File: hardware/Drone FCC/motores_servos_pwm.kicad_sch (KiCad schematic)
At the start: 13 parts, among them J10 Conn_01x03, J11 Conn_01x03, J12 Conn_01x03, J13 Conn_01x03, J14 Conn_01x03, J16 Conn_01x02, J3 Conn_01x03, J4 Conn_01x03, J5 Conn_01x03, J6 Conn_01x03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

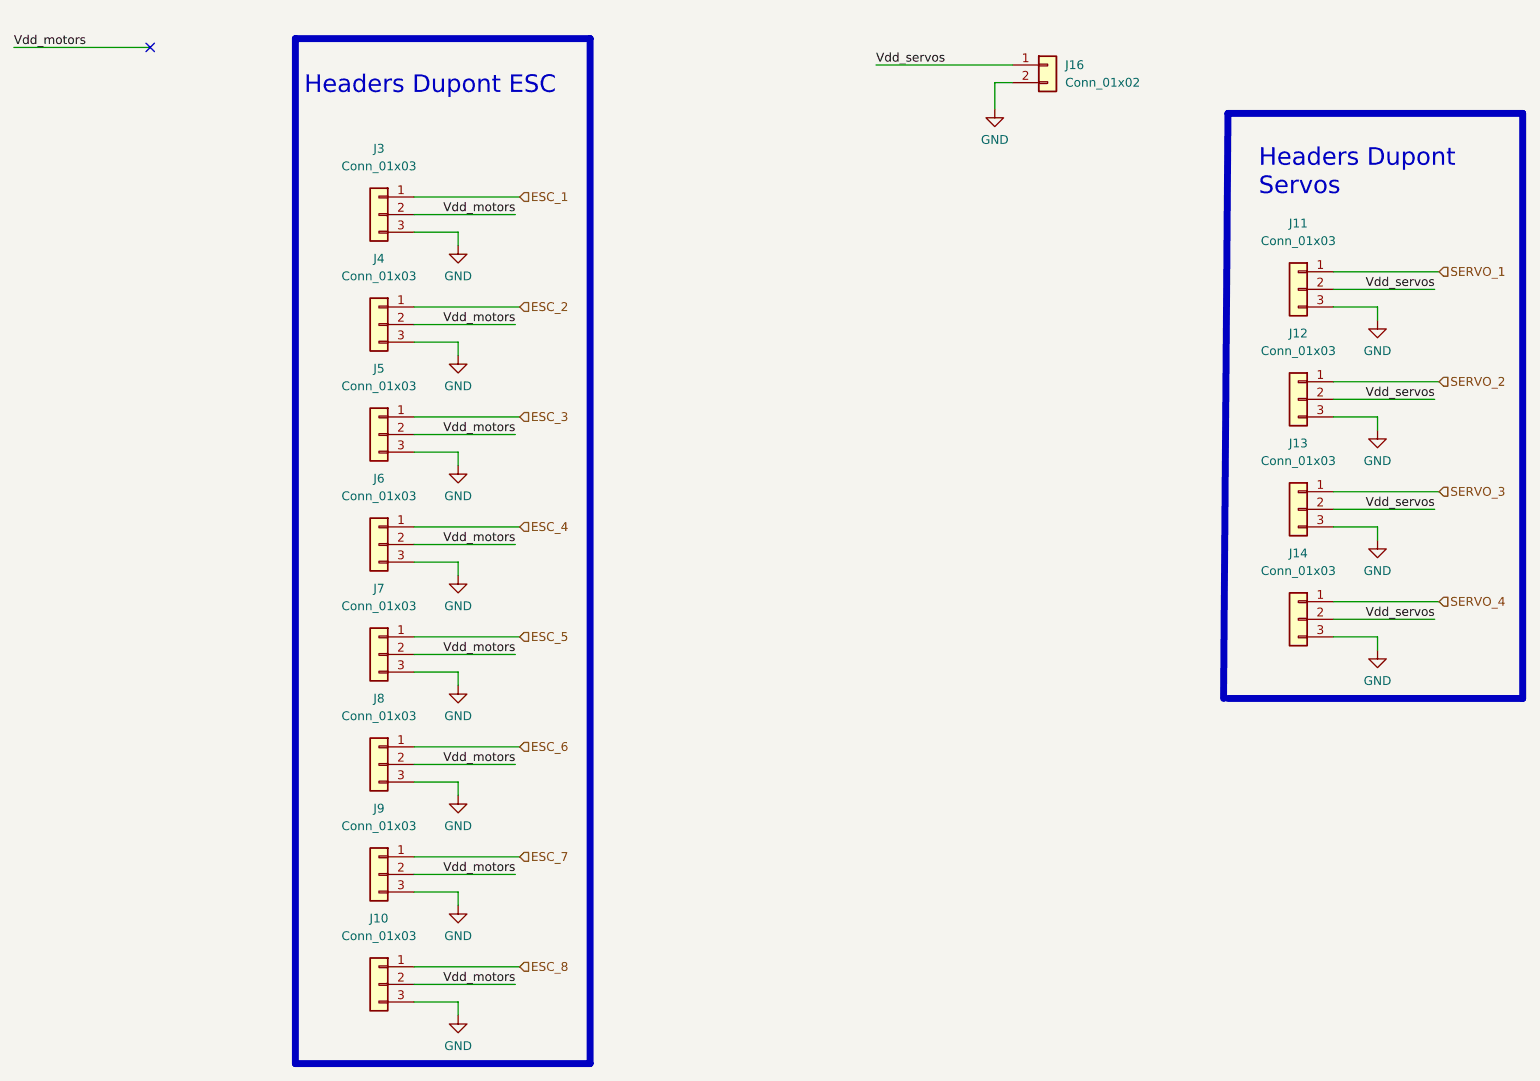
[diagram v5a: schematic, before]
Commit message: re enumeration of components
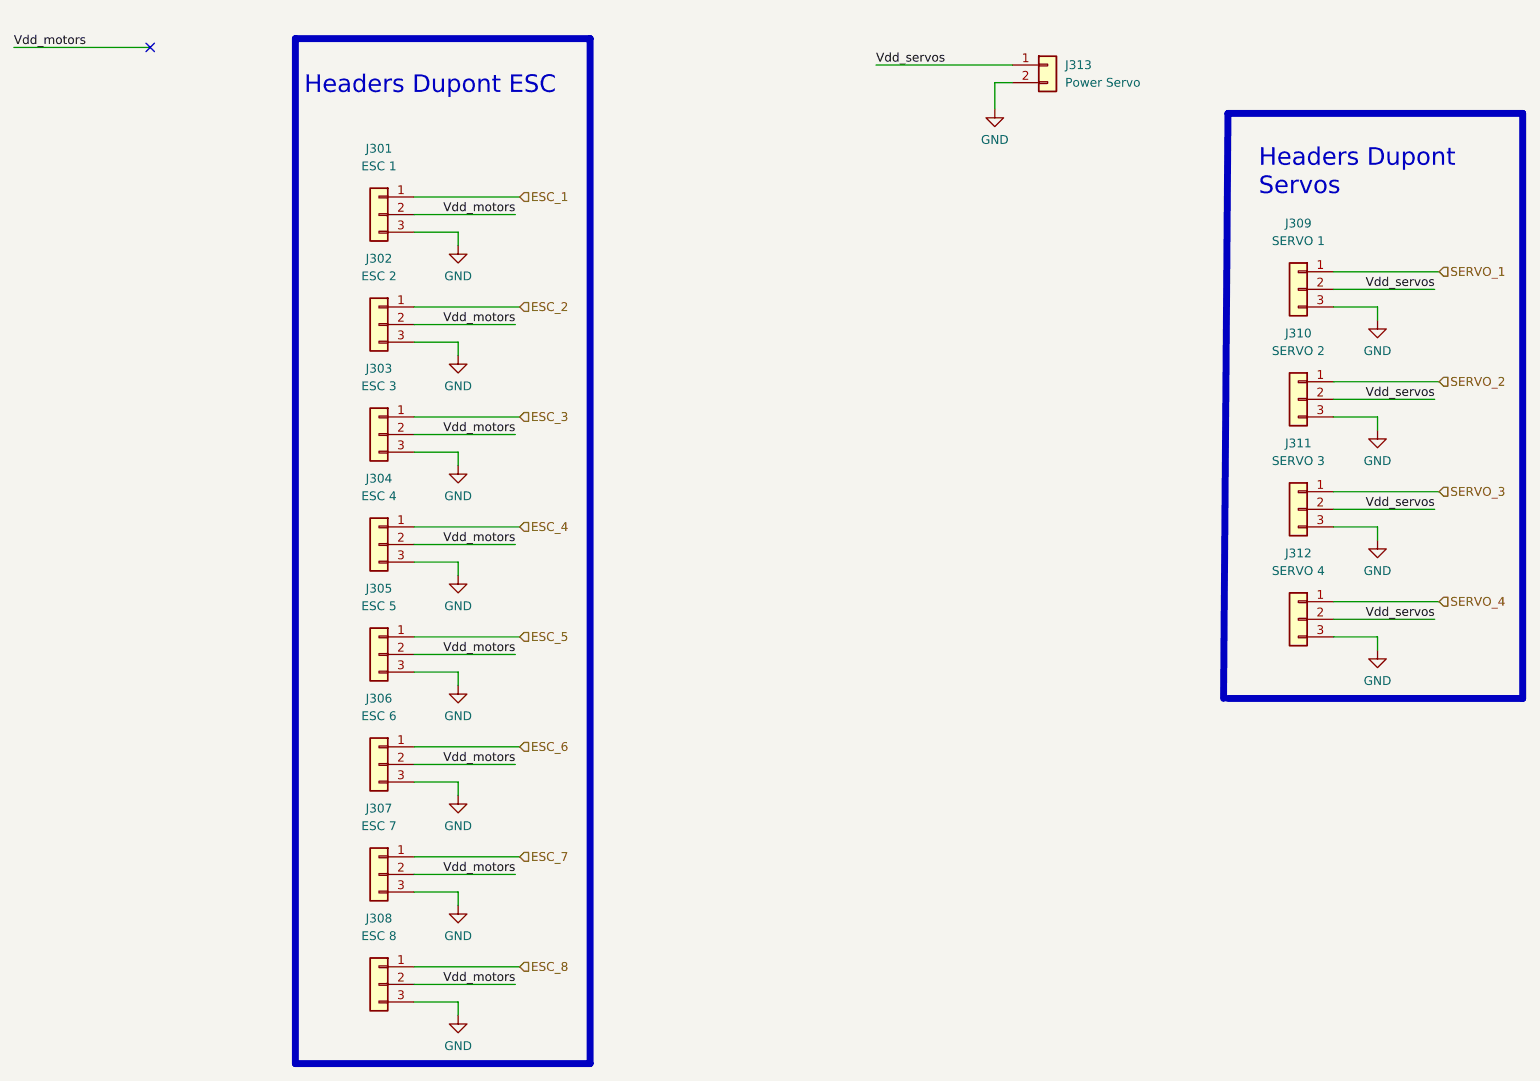
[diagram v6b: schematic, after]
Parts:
- J301: renamed from J3; value Conn_01x03 -> ESC 1
- J302: renamed from J4; value Conn_01x03 -> ESC 2
- J303: renamed from J5; value Conn_01x03 -> ESC 3
- J304: renamed from J6; value Conn_01x03 -> ESC 4
- J305: renamed from J7; value Conn_01x03 -> ESC 5
- J306: renamed from J8; value Conn_01x03 -> ESC 6
- J307: renamed from J9; value Conn_01x03 -> ESC 7
- J308: renamed from J10; value Conn_01x03 -> ESC 8
- J309: renamed from J11; value Conn_01x03 -> SERVO 1
- J310: renamed from J12; value Conn_01x03 -> SERVO 2
- J311: renamed from J13; value Conn_01x03 -> SERVO 3
- J312: renamed from J14; value Conn_01x03 -> SERVO 4
- J313: renamed from J16; value Conn_01x02 -> Power Servo
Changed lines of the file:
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@@
   (symbol (lib_id "Connector_Generic:Conn_01x03") (at 201.295 89.535 0) (mirror y) (unit 1)
     (in_bom yes) (on_board yes) (fields_autoplaced)
-    (property "Reference" "J13" (id 0) (at 201.295 80.01 0))
-    (property "Value" "Conn_01x03" (id 1) (at 201.295 82.55 0))
+    (property "Reference" "J311" (id 0) (at 201.295 80.01 0))
+    (property "Value" "SERVO 3" (id 1) (at 201.295 82.55 0))
     (property "Footprint" "TSW-101-08-G-T-RA:SAMTEC_TSW-101-08-G-T-RA" (id 2) (at 201.295 89.535 0)
       (effects (font (size 1.27 1.27)) hide)
@@
   (symbol (lib_id "Connector_Generic:Conn_01x03") (at 68.58 110.49 0) (mirror y) (unit 1)
     (in_bom yes) (on_board yes) (fields_autoplaced)
-    (property "Reference" "J7" (id 0) (at 68.58 100.965 0))
-    (property "Value" "Conn_01x03" (id 1) (at 68.58 103.505 0))
+    (property "Reference" "J305" (id 0) (at 68.58 100.965 0))
+    (property "Value" "ESC 5" (id 1) (at 68.58 103.505 0))
     (property "Footprint" "TSW-101-08-G-T-RA:SAMTEC_TSW-101-08-G-T-RA" (id 2) (at 68.58 110.49 0)
       (effects (font (size 1.27 1.27)) hide)
@@
   (symbol (lib_id "Connector_Generic:Conn_01x03") (at 68.58 46.99 0) (mirror y) (unit 1)
     (in_bom yes) (on_board yes) (fields_autoplaced)
-    (property "Reference" "J3" (id 0) (at 68.58 37.465 0))
-    (property "Value" "Conn_01x03" (id 1) (at 68.58 40.005 0))
+    (property "Reference" "J301" (id 0) (at 68.58 37.465 0))
+    (property "Value" "ESC 1" (id 1) (at 68.58 40.005 0))
     (property "Footprint" "TSW-101-08-G-T-RA:SAMTEC_TSW-101-08-G-T-RA" (id 2) (at 68.58 46.99 0)
       (effects (font (size 1.27 1.27)) hide)
@@
   (symbol (lib_id "Connector_Generic:Conn_01x03") (at 68.58 62.865 0) (mirror y) (unit 1)
     (in_bom yes) (on_board yes) (fields_autoplaced)
-    (property "Reference" "J4" (id 0) (at 68.58 53.34 0))
-    (property "Value" "Conn_01x03" (id 1) (at 68.58 55.88 0))
+    (property "Reference" "J302" (id 0) (at 68.58 53.34 0))
+    (property "Value" "ESC 2" (id 1) (at 68.58 55.88 0))
     (property "Footprint" "TSW-101-08-G-T-RA:SAMTEC_TSW-101-08-G-T-RA" (id 2) (at 68.58 62.865 0)
       (effects (font (size 1.27 1.27)) hide)
@@
   (symbol (lib_id "Connector_Generic:Conn_01x03") (at 201.295 105.41 0) (mirror y) (unit 1)
     (in_bom yes) (on_board yes) (fields_autoplaced)
-    (property "Reference" "J14" (id 0) (at 201.295 95.885 0))
-    (property "Value" "Conn_01x03" (id 1) (at 201.295 98.425 0))
+    (property "Reference" "J312" (id 0) (at 201.295 95.885 0))
+    (property "Value" "SERVO 4" (id 1) (at 201.295 98.425 0))
     (property "Footprint" "TSW-101-08-G-T-RA:SAMTEC_TSW-101-08-G-T-RA" (id 2) (at 201.295 105.41 0)
       (effects (font (size 1.27 1.27)) hide)
@@
   (symbol (lib_id "Connector_Generic:Conn_01x03") (at 68.58 78.74 0) (mirror y) (unit 1)
     (in_bom yes) (on_board yes) (fields_autoplaced)
-    (property "Reference" "J5" (id 0) (at 68.58 69.215 0))
-    (property "Value" "Conn_01x03" (id 1) (at 68.58 71.755 0))
+    (property "Reference" "J303" (id 0) (at 68.58 69.215 0))
+    (property "Value" "ESC 3" (id 1) (at 68.58 71.755 0))
     (property "Footprint" "TSW-101-08-G-T-RA:SAMTEC_TSW-101-08-G-T-RA" (id 2) (at 68.58 78.74 0)
       (effects (font (size 1.27 1.27)) hide)
@@
   (symbol (lib_id "Connector_Generic:Conn_01x03") (at 201.295 57.785 0) (mirror y) (unit 1)
     (in_bom yes) (on_board yes)
-    (property "Reference" "J11" (id 0) (at 201.295 48.26 0))
-    (property "Value" "Conn_01x03" (id 1) (at 201.295 50.8 0))
+    (property "Reference" "J309" (id 0) (at 201.295 48.26 0))
+    (property "Value" "SERVO 1" (id 1) (at 201.295 50.8 0))
     (property "Footprint" "TSW-101-08-G-T-RA:SAMTEC_TSW-101-08-G-T-RA" (id 2) (at 201.295 57.785 0)
       (effects (font (size 1.27 1.27)) hide)
@@
   (symbol (lib_id "Connector_Generic:Conn_01x03") (at 68.58 94.615 0) (mirror y) (unit 1)
     (in_bom yes) (on_board yes) (fields_autoplaced)
-    (property "Reference" "J6" (id 0) (at 68.58 85.09 0))
-    (property "Value" "Conn_01x03" (id 1) (at 68.58 87.63 0))
+    (property "Reference" "J304" (id 0) (at 68.58 85.09 0))
+    (property "Value" "ESC 4" (id 1) (at 68.58 87.63 0))
     (property "Footprint" "TSW-101-08-G-T-RA:SAMTEC_TSW-101-08-G-T-RA" (id 2) (at 68.58 94.615 0)
       (effects (font (size 1.27 1.27)) hide)
@@
   (symbol (lib_id "Connector_Generic:Conn_01x03") (at 68.58 158.115 0) (mirror y) (unit 1)
     (in_bom yes) (on_board yes) (fields_autoplaced)
-    (property "Reference" "J10" (id 0) (at 68.58 148.59 0))
-    (property "Value" "Conn_01x03" (id 1) (at 68.58 151.13 0))
+    (property "Reference" "J308" (id 0) (at 68.58 148.59 0))
+    (property "Value" "ESC 8" (id 1) (at 68.58 151.13 0))
     (property "Footprint" "TSW-101-08-G-T-RA:SAMTEC_TSW-101-08-G-T-RA" (id 2) (at 68.58 158.115 0)
       (effects (font (size 1.27 1.27)) hide)
@@
   (symbol (lib_id "Connector_Generic:Conn_01x02") (at 165.1 25.4 0) (unit 1)
     (in_bom yes) (on_board yes) (fields_autoplaced)
-    (property "Reference" "J16" (id 0) (at 167.64 25.3999 0)
+    (property "Reference" "J313" (id 0) (at 167.64 25.3999 0)
       (effects (font (size 1.27 1.27)) (justify left))
     )
-    (property "Value" "Conn_01x02" (id 1) (at 167.64 27.9399 0)
+    (property "Value" "Power Servo" (id 1) (at 167.64 27.9399 0)
       (effects (font (size 1.27 1.27)) (justify left))
     )
@@
   (symbol (lib_id "Connector_Generic:Conn_01x03") (at 68.58 142.24 0) (mirror y) (unit 1)
     (in_bom yes) (on_board yes) (fields_autoplaced)
-    (property "Reference" "J9" (id 0) (at 68.58 132.715 0))
-    (property "Value" "Conn_01x03" (id 1) (at 68.58 135.255 0))
+    (property "Reference" "J307" (id 0) (at 68.58 132.715 0))
+    (property "Value" "ESC 7" (id 1) (at 68.58 135.255 0))
     (property "Footprint" "TSW-101-08-G-T-RA:SAMTEC_TSW-101-08-G-T-RA" (id 2) (at 68.58 142.24 0)
       (effects (font (size 1.27 1.27)) hide)
@@
   (symbol (lib_id "Connector_Generic:Conn_01x03") (at 68.58 126.365 0) (mirror y) (unit 1)
     (in_bom yes) (on_board yes) (fields_autoplaced)
-    (property "Reference" "J8" (id 0) (at 68.58 116.84 0))
-    (property "Value" "Conn_01x03" (id 1) (at 68.58 119.38 0))
+    (property "Reference" "J306" (id 0) (at 68.58 116.84 0))
+    (property "Value" "ESC 6" (id 1) (at 68.58 119.38 0))
     (property "Footprint" "TSW-101-08-G-T-RA:SAMTEC_TSW-101-08-G-T-RA" (id 2) (at 68.58 126.365 0)
       (effects (font (size 1.27 1.27)) hide)
@@
   (symbol (lib_id "Connector_Generic:Conn_01x03") (at 201.295 73.66 0) (mirror y) (unit 1)
     (in_bom yes) (on_board yes) (fields_autoplaced)
-    (property "Reference" "J12" (id 0) (at 201.295 64.135 0))
-    (property "Value" "Conn_01x03" (id 1) (at 201.295 66.675 0))
+    (property "Reference" "J310" (id 0) (at 201.295 64.135 0))
+    (property "Value" "SERVO 2" (id 1) (at 201.295 66.675 0))
     (property "Footprint" "TSW-101-08-G-T-RA:SAMTEC_TSW-101-08-G-T-RA" (id 2) (at 201.295 73.66 0)
       (effects (font (size 1.27 1.27)) hide)

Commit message: continued preliminar routing
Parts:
- J313: footprint Connector_Phoenix_MSTB:PhoenixContact_MSTBA_2,5_2-G-5,08_1x02_P5.08mm_Horizontal -> 1935161:PHOENIX_1935161
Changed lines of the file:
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@@
       (effects (font (size 1.27 1.27)) (justify left))
     )
-    (property "Footprint" "Connector_Phoenix_MSTB:PhoenixContact_MSTBA_2,5_2-G-5,08_1x02_P5.08mm_Horizontal" (id 2) (at 165.1 25.4 0)
+    (property "Footprint" "1935161:PHOENIX_1935161" (id 2) (at 165.1 25.4 0)
       (effects (font (size 1.27 1.27)) hide)
     )

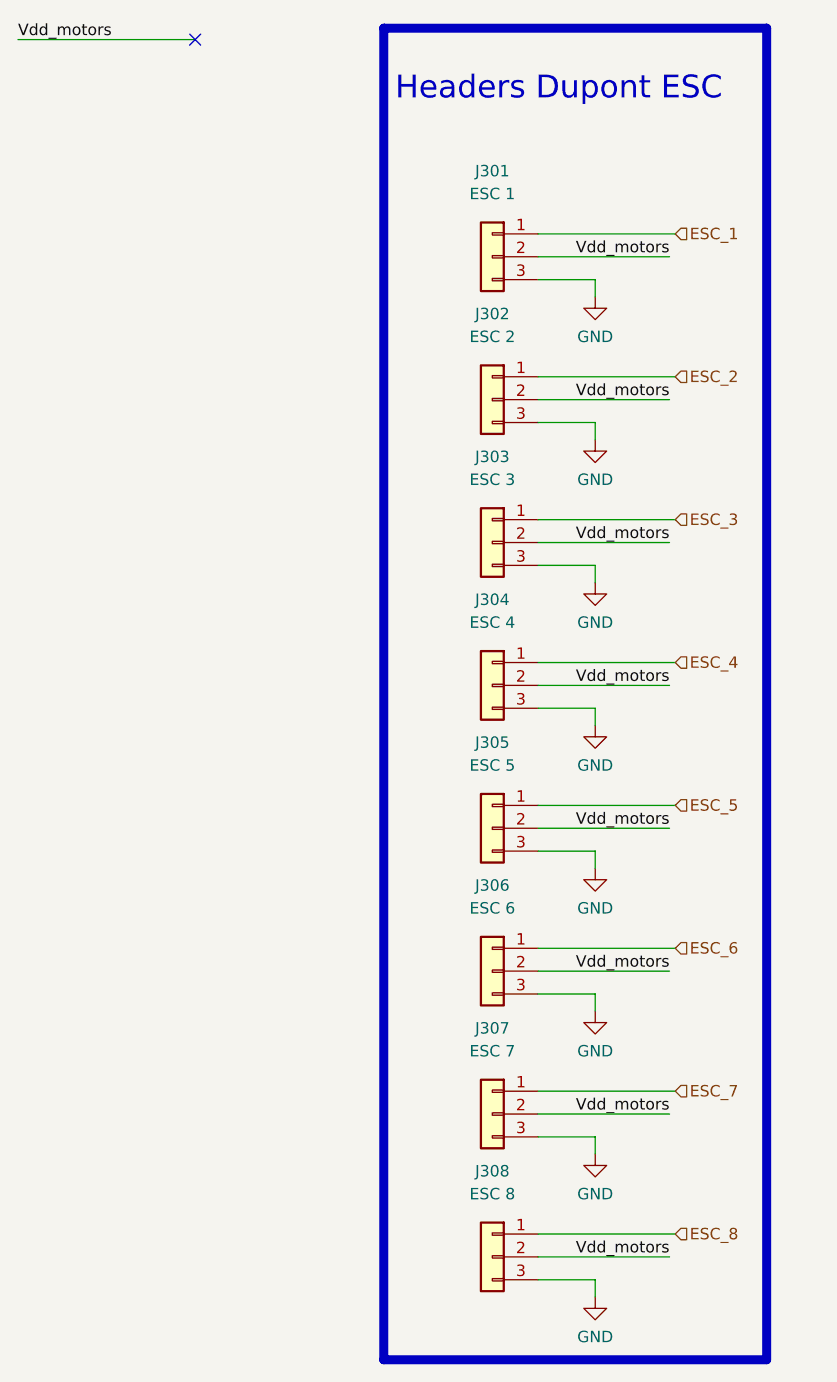
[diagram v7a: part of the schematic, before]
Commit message: LDO layout on PCB
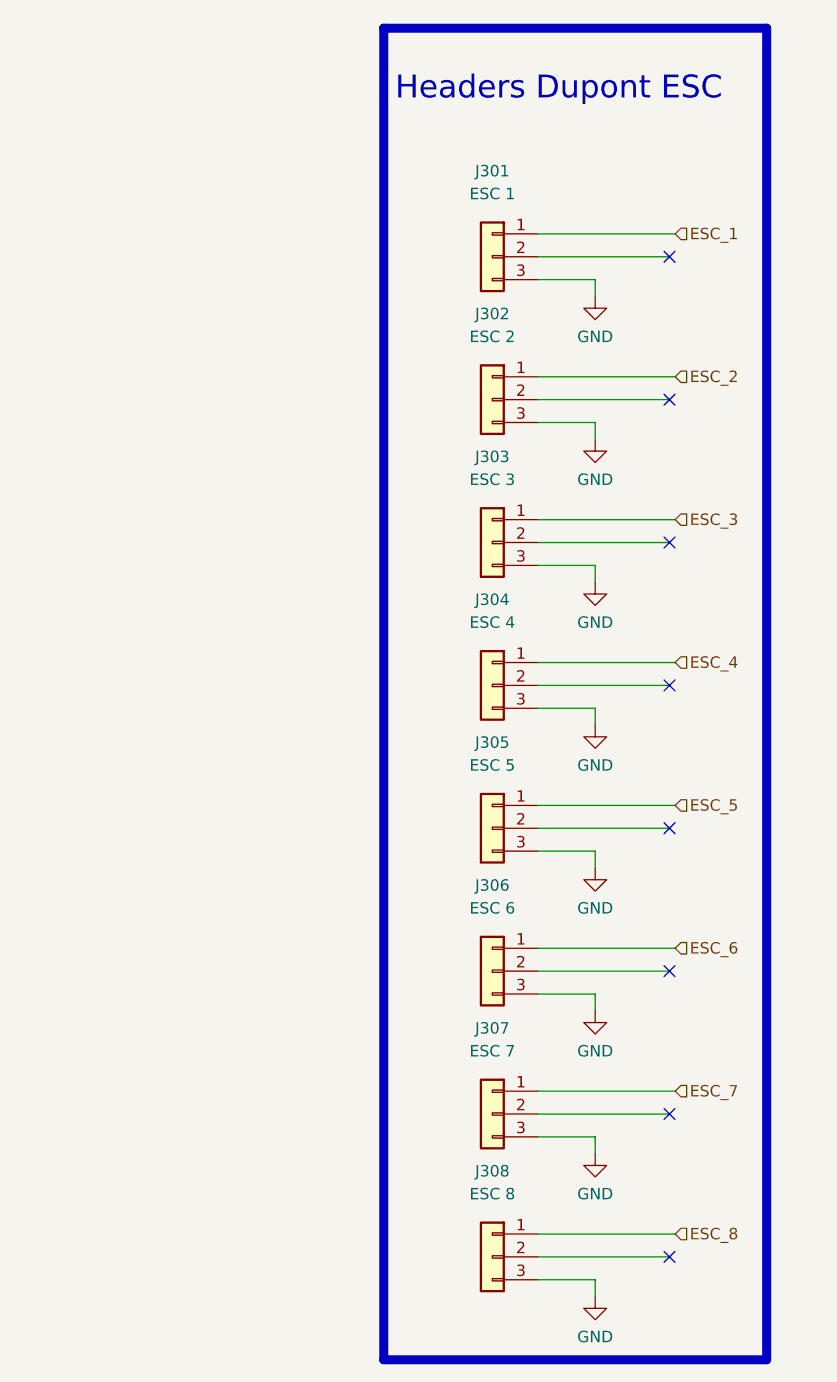
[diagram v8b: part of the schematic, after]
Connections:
- removed net Vdd_motors: J301.2 (Pin_2), J302.2 (Pin_2), J303.2 (Pin_2), J304.2 (Pin_2), J305.2 (Pin_2), J306.2 (Pin_2), J307.2 (Pin_2), J308.2 (Pin_2)
- no-connect marks 1 -> 8
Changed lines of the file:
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@@
 (kicad_sch (version 20211123) (generator eeschema)
   (paper "A4")
-  (no_connect (at 35.56 22.86))
+  (no_connect (at 88.265 126.365))
+  (no_connect (at 88.265 110.49))
+  (no_connect (at 88.265 158.115))
+  (no_connect (at 88.265 46.99))
+  (no_connect (at 88.265 62.865))
+  (no_connect (at 88.265 78.74))
+  (no_connect (at 88.265 94.615))
+  (no_connect (at 88.265 142.24))
   (wire (pts (xy 212.725 78.105) (xy 212.725 76.2))
     (stroke (width 0) (type default) (color 0 0 0 0))
@@
   (polyline (pts (xy 56.515 21.59) (xy 99.06 21.59))
     (stroke (width 1) (type default) (color 0 0 0 0))
-  )
-  (wire (pts (xy 15.875 22.86) (xy 35.56 22.86))
-    (stroke (width 0) (type default) (color 0 0 0 0))
   )
   (wire (pts (xy 160.02 27.94) (xy 157.48 27.94))
@@
     (effects (font (size 2.54 2.54)) (justify left bottom))
   )
-  (label "Vdd_motors" (at 88.265 142.24 180)
-    (effects (font (size 1.27 1.27)) (justify right bottom))
-  )
-  (label "Vdd_motors" (at 88.265 126.365 180)
+  (label "Vdd_servos" (at 220.98 89.535 180)
+    (effects (font (size 1.27 1.27)) (justify right bottom))
+  )
+  (label "Vdd_servos" (at 220.98 105.41 180)
+    (effects (font (size 1.27 1.27)) (justify right bottom))
+  )
+  (label "Vdd_servos" (at 220.98 57.785 180)
     (effects (font (size 1.27 1.27)) (justify right bottom))
   )
@@
     (effects (font (size 1.27 1.27)) (justify left bottom))
   )
-  (label "Vdd_motors" (at 88.265 62.865 180)
-    (effects (font (size 1.27 1.27)) (justify right bottom))
-  )
-  (label "Vdd_servos" (at 220.98 89.535 180)
-    (effects (font (size 1.27 1.27)) (justify right bottom))
-  )
-  (label "Vdd_motors" (at 88.265 78.74 180)
-    (effects (font (size 1.27 1.27)) (justify right bottom))
-  )
-  (label "Vdd_servos" (at 220.98 105.41 180)
-    (effects (font (size 1.27 1.27)) (justify right bottom))
-  )
-  (label "Vdd_motors" (at 88.265 46.99 180)
-    (effects (font (size 1.27 1.27)) (justify right bottom))
-  )
-  (label "Vdd_motors" (at 88.265 94.615 180)
-    (effects (font (size 1.27 1.27)) (justify right bottom))
-  )
-  (label "Vdd_servos" (at 220.98 57.785 180)
-    (effects (font (size 1.27 1.27)) (justify right bottom))
-  )
-  (label "Vdd_motors" (at 15.875 22.86 0)
-    (effects (font (size 1.27 1.27)) (justify left bottom))
-  )
-  (label "Vdd_motors" (at 88.265 158.115 180)
-    (effects (font (size 1.27 1.27)) (justify right bottom))
-  )
-  (label "Vdd_motors" (at 88.265 110.49 180)
-    (effects (font (size 1.27 1.27)) (justify right bottom))
-  )
   (hierarchical_label "ESC_5" (shape input) (at 88.9 107.95 0)
